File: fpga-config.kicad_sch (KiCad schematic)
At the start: 22 parts, among them J1 878321412, Q1 BSS138W-7-F, Q2 BSS138W-7-F, SW1 CVS-03B, U1 XC7K410T-2FFG900I, U2 TPD4E05U06QDQARQ1, U3 MAX1617AMEE+T

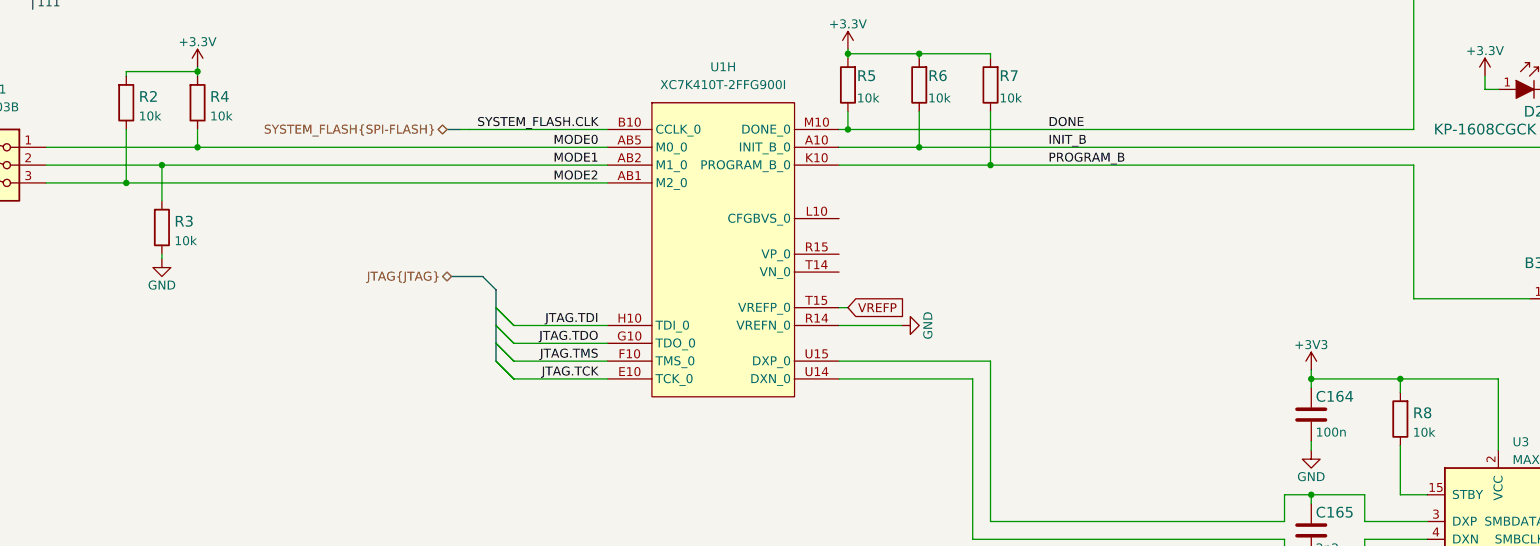
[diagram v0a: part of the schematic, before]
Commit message: Add new pinout to sup MCU. Start connecting it to FPGA
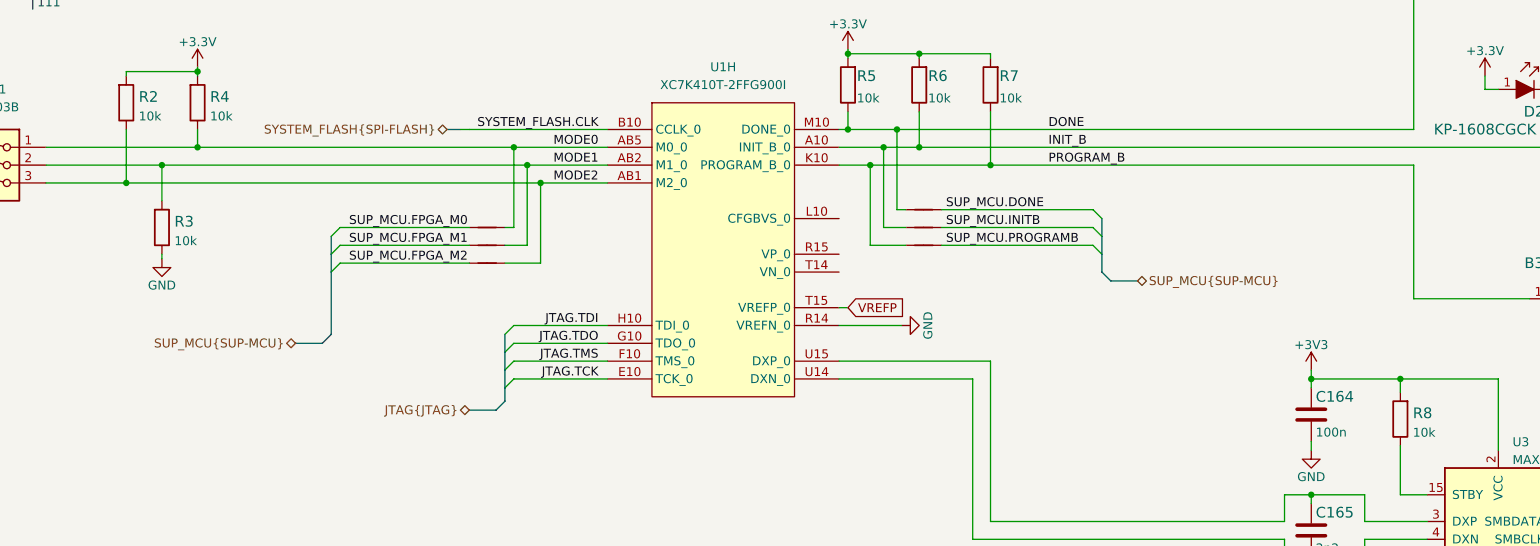
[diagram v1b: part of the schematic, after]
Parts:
- added NT? (x6): NetTie_2, antmicro-footprints:NetTie-2_SMD_Pad0.127mm, symbol antmicroShuntsJumpers:NetTie_2
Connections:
- net DONE: now also NT?.2
- net INIT_B: now also NT?.2
- net MODE0: now also NT?.2
- net MODE1: now also NT?.2
- net MODE2: now also NT?.2
- net PROGRAM_B: now also NT?.2
- new net SUP_MCU.DONE: NT?.1
- new net SUP_MCU.FPGA_M0: NT?.1
- new net SUP_MCU.FPGA_M1: NT?.1
- new net SUP_MCU.FPGA_M2: NT?.1
- new net SUP_MCU.INITB: NT?.1
- new net SUP_MCU.PROGRAMB: NT?.1

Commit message: Add DDR3L decoupling capacitors
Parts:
- gave numbers to parts that had none: 6
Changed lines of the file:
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@@
   (symbol (lib_id "antmicroShuntsJumpers:NetTie_2") (at 182.245 142.24 0) (unit 1)
     (in_bom yes) (on_board yes) (fields_autoplaced)
-    (property "Reference" "NT?" (id 0) (at 182.245 140.97 0)
+    (property "Reference" "NT3" (id 0) (at 182.245 140.97 0)
       (effects (font (size 1.27 1.27)) hide)
     )
@@
   (symbol (lib_id "antmicroShuntsJumpers:NetTie_2") (at 182.245 147.32 0) (unit 1)
     (in_bom yes) (on_board yes) (fields_autoplaced)
-    (property "Reference" "NT?" (id 0) (at 182.245 146.05 0)
+    (property "Reference" "NT5" (id 0) (at 182.245 146.05 0)
       (effects (font (size 1.27 1.27)) hide)
     )
@@
   (symbol (lib_id "antmicroShuntsJumpers:NetTie_2") (at 244.475 139.7 0) (mirror y) (unit 1)
     (in_bom yes) (on_board yes) (fields_autoplaced)
-    (property "Reference" "NT?" (id 0) (at 244.475 138.43 0)
+    (property "Reference" "NT6" (id 0) (at 244.475 138.43 0)
       (effects (font (size 1.27 1.27)) hide)
     )
@@
   (symbol (lib_id "antmicroShuntsJumpers:NetTie_2") (at 244.475 144.78 0) (mirror y) (unit 1)
     (in_bom yes) (on_board yes) (fields_autoplaced)
-    (property "Reference" "NT?" (id 0) (at 244.475 143.51 0)
+    (property "Reference" "NT8" (id 0) (at 244.475 143.51 0)
       (effects (font (size 1.27 1.27)) hide)
     )
@@
   (symbol (lib_id "antmicroShuntsJumpers:NetTie_2") (at 182.245 144.78 0) (unit 1)
     (in_bom yes) (on_board yes) (fields_autoplaced)
-    (property "Reference" "NT?" (id 0) (at 182.245 143.51 0)
+    (property "Reference" "NT4" (id 0) (at 182.245 143.51 0)
       (effects (font (size 1.27 1.27)) hide)
     )
@@
   (symbol (lib_id "antmicroShuntsJumpers:NetTie_2") (at 244.475 142.24 0) (mirror y) (unit 1)
     (in_bom yes) (on_board yes) (fields_autoplaced)
-    (property "Reference" "NT?" (id 0) (at 244.475 140.97 0)
-      (effects (font (size 1.27 1.27)) hide)
-    )
+    (property "Reference" "NT7" (id 0) (at 244.475 140.97 0)
+      (effects (font (size 1.27 1.27)) hide)
+    )

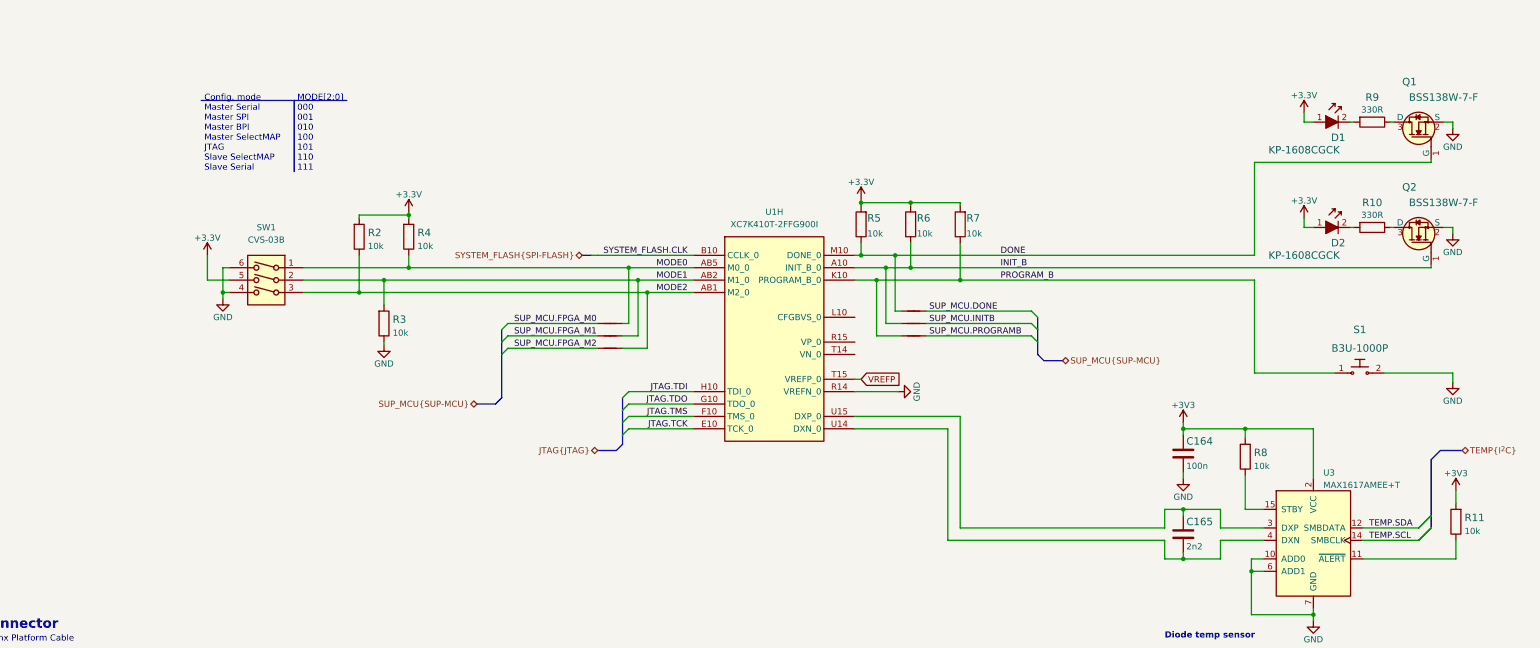
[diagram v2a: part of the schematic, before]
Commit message: Connect SUP MCU CLCK signal to FPGA
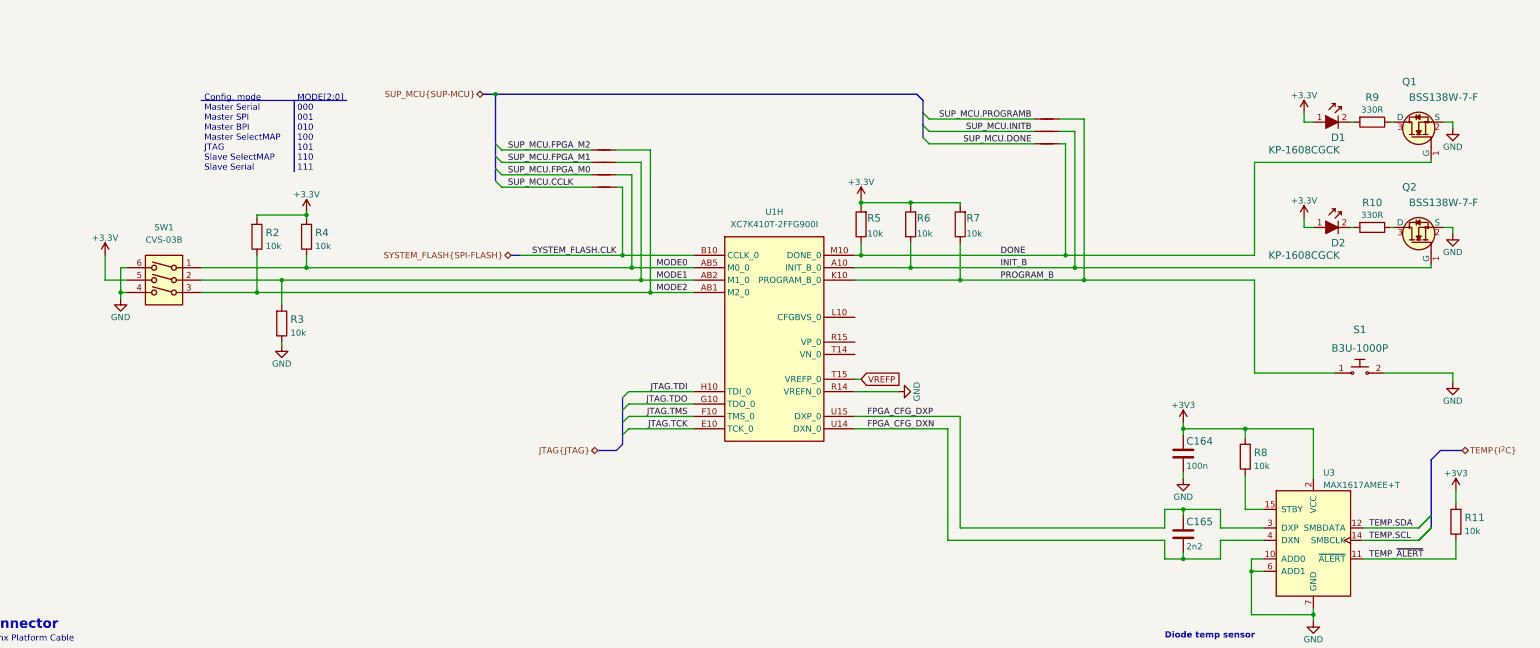
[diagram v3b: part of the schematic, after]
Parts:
- added NT?: NetTie_2, antmicro-footprints:NetTie-2_SMD_Pad0.127mm, symbol antmicroShuntsJumpers:NetTie_2
- renumbered NT3 to NT?, NT5 to NT?, NT6 to NT?, NT8 to NT?, NT4 to NT?, NT7 to NT?
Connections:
- net SYSTEM_FLASH.CLK: now also NT?.2
- net TEMP_~{ALERT}: now reaches R11.1, U3.11 (~{ALERT})
- net FPGA_CFG_DXP: now reaches C165.1, U1.U15 (DXP_0), U3.3 (DXP)
- net FPGA_CFG_DXN: now reaches C165.2, U1.U14 (DXN_0), U3.4 (DXN)
- new net SUP_MCU.CCLK: NT?.1
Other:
- moved on the sheet: R2, R3, R4, SW1

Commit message: Fix DDR3L placement
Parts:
- gave numbers to parts that had none: 7
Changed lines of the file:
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@@
   (symbol (lib_id "antmicroShuntsJumpers:NetTie_2") (at 180.975 111.76 0) (mirror x) (unit 1)
     (in_bom yes) (on_board yes) (fields_autoplaced)
-    (property "Reference" "NT?" (id 0) (at 180.975 113.03 0)
+    (property "Reference" "NT3" (id 0) (at 180.975 113.03 0)
       (effects (font (size 1.27 1.27)) hide)
     )
@@
   (symbol (lib_id "antmicroShuntsJumpers:NetTie_2") (at 180.975 114.3 0) (mirror x) (unit 1)
     (in_bom yes) (on_board yes) (fields_autoplaced)
-    (property "Reference" "NT?" (id 0) (at 180.975 115.57 0)
+    (property "Reference" "NT19" (id 0) (at 180.975 115.57 0)
       (effects (font (size 1.27 1.27)) hide)
     )
@@
   (symbol (lib_id "antmicroShuntsJumpers:NetTie_2") (at 180.975 106.68 0) (mirror x) (unit 1)
     (in_bom yes) (on_board yes) (fields_autoplaced)
-    (property "Reference" "NT?" (id 0) (at 180.975 107.95 0)
+    (property "Reference" "NT5" (id 0) (at 180.975 107.95 0)
       (effects (font (size 1.27 1.27)) hide)
     )
@@
   (symbol (lib_id "antmicroShuntsJumpers:NetTie_2") (at 271.78 105.41 0) (mirror x) (unit 1)
     (in_bom yes) (on_board yes) (fields_autoplaced)
-    (property "Reference" "NT?" (id 0) (at 271.78 106.68 0)
+    (property "Reference" "NT6" (id 0) (at 271.78 106.68 0)
       (effects (font (size 1.27 1.27)) hide)
     )
@@
   (symbol (lib_id "antmicroShuntsJumpers:NetTie_2") (at 271.78 100.33 0) (mirror x) (unit 1)
     (in_bom yes) (on_board yes) (fields_autoplaced)
-    (property "Reference" "NT?" (id 0) (at 271.78 101.6 0)
+    (property "Reference" "NT8" (id 0) (at 271.78 101.6 0)
       (effects (font (size 1.27 1.27)) hide)
     )
@@
   (symbol (lib_id "antmicroShuntsJumpers:NetTie_2") (at 180.975 109.22 0) (mirror x) (unit 1)
     (in_bom yes) (on_board yes) (fields_autoplaced)
-    (property "Reference" "NT?" (id 0) (at 180.975 110.49 0)
+    (property "Reference" "NT4" (id 0) (at 180.975 110.49 0)
       (effects (font (size 1.27 1.27)) hide)
     )
@@
   (symbol (lib_id "antmicroShuntsJumpers:NetTie_2") (at 271.78 102.87 0) (mirror x) (unit 1)
     (in_bom yes) (on_board yes) (fields_autoplaced)
-    (property "Reference" "NT?" (id 0) (at 271.78 104.14 0)
-      (effects (font (size 1.27 1.27)) hide)
-    )
+    (property "Reference" "NT7" (id 0) (at 271.78 104.14 0)
+      (effects (font (size 1.27 1.27)) hide)
+    )

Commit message: Finish connecting MCU
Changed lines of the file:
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@@
     (stroke (width 0) (type default) (color 0 0 0 0))
   )
-  (bus_entry (at 350.52 181.61) (size -2.54 2.54)
+  (bus_entry (at 350.52 182.88) (size -1.27 1.27)
     (stroke (width 0) (type default) (color 0 0 0 0))
   )
@@
     (stroke (width 0) (type default) (color 0 0 0 0))
   )
-  (bus_entry (at 350.52 181.61) (size -2.54 2.54)
-    (stroke (width 0) (type default) (color 0 0 0 0))
-  )
   (bus_entry (at 184.785 160.02) (size 1.27 -1.27)
     (stroke (width 0) (type default) (color 0 0 0 0))
@@
     (stroke (width 0) (type default) (color 0 0 0 0))
   )
-  (bus_entry (at 350.52 184.15) (size -2.54 2.54)
-    (stroke (width 0) (type default) (color 0 0 0 0))
-  )
   (bus_entry (at 86.36 229.87) (size -2.54 2.54)
     (stroke (width 0) (type default) (color 0 0 0 0))
   )
-  (bus_entry (at 350.52 184.15) (size -2.54 2.54)
+  (bus_entry (at 350.52 185.42) (size -1.27 1.27)
     (stroke (width 0) (type default) (color 0 0 0 0))
   )
@@
     (stroke (width 0) (type default) (color 0 0 0 0))
   )
-  (bus (pts (xy 350.52 181.61) (xy 350.52 184.15))
-    (stroke (width 0) (type default) (color 0 0 0 0))
-  )
   (wire (pts (xy 307.34 180.34) (xy 299.72 180.34))
     (stroke (width 0) (type default) (color 0 0 0 0))
@@
     (stroke (width 0) (type default) (color 0 0 0 0))
   )
-  (bus (pts (xy 350.52 170.18) (xy 350.52 181.61))
+  (bus (pts (xy 350.52 170.18) (xy 350.52 182.88))
     (stroke (width 0) (type default) (color 0 0 0 0))
   )
@@
     (stroke (width 0.1016) (type solid) (color 0 0 0 0))
   )
-  (wire (pts (xy 336.55 186.69) (xy 347.98 186.69))
+  (bus (pts (xy 350.52 182.88) (xy 350.52 185.42))
+    (stroke (width 0) (type default) (color 0 0 0 0))
+  )
+  (wire (pts (xy 336.55 186.69) (xy 349.25 186.69))
     (stroke (width 0) (type default) (color 0 0 0 0))
   )
@@
     (stroke (width 0) (type default) (color 0 0 0 0))
   )
-  (wire (pts (xy 336.55 184.15) (xy 347.98 184.15))
-    (stroke (width 0) (type default) (color 0 0 0 0))
-  )
+  (wire (pts (xy 336.55 184.15) (xy 349.25 184.15))
+    (stroke (width 0) (type default) (color 0 0 0 0))
+  )

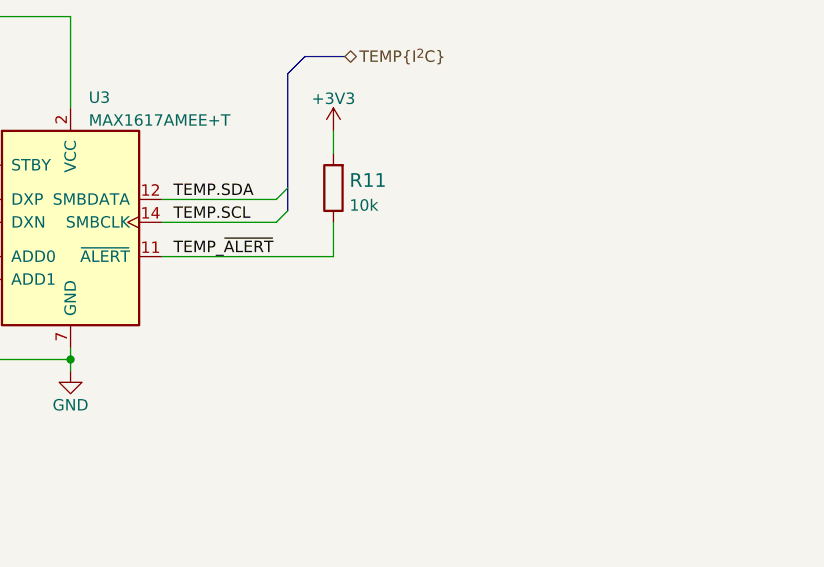
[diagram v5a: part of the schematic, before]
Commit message: Connect TEMP_ALERT_N signal to MCU
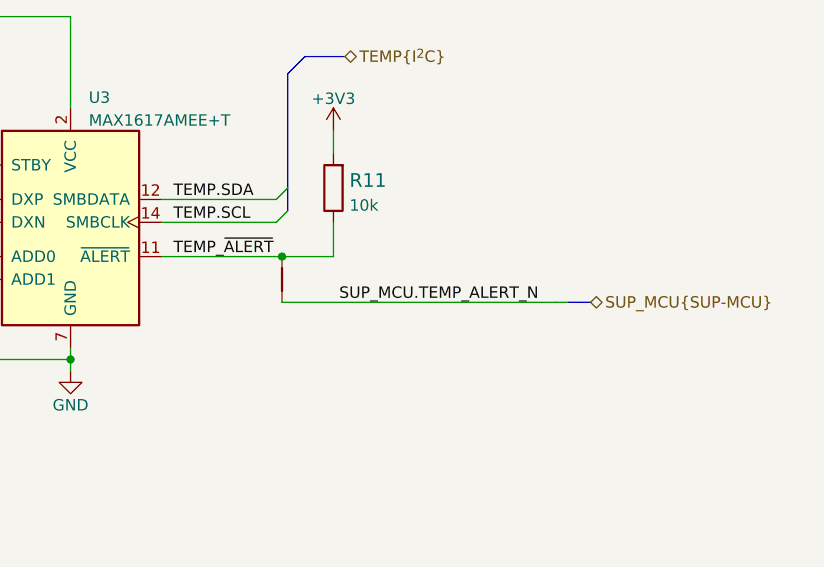
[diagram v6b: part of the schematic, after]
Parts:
- added NT?: NetTie_2, antmicro-footprints:NetTie-2_SMD_Pad0.127mm, symbol antmicroShuntsJumpers:NetTie_2
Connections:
- net TEMP_~{ALERT}: now also NT?.2
- new net SUP_MCU.TEMP_ALERT_N: NT?.1
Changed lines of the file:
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@@
   (junction (at 114.935 133.35) (diameter 0) (color 0 0 0 0)
+  )
+  (junction (at 349.885 190.5) (diameter 0) (color 0 0 0 0)
   )
   (junction (at 313.69 193.04) (diameter 0) (color 0 0 0 0)
@@
     (stroke (width 0) (type default) (color 0 0 0 0))
   )
+  (bus_entry (at 380.365 195.58) (size 1.27 0)
+    (stroke (width 0) (type default) (color 0 0 0 0))
+  )
   (bus_entry (at 158.75 113.03) (size 1.27 1.27)
     (stroke (width 0) (type default) (color 0 0 0 0))
@@
     (stroke (width 0) (type default) (color 0 0 0 0))
   )
-  (wire (pts (xy 336.55 190.5) (xy 355.6 190.5))
+  (wire (pts (xy 336.55 190.5) (xy 349.885 190.5))
     (stroke (width 0) (type default) (color 0 0 0 0))
   )
@@
     (stroke (width 0) (type default) (color 0 0 0 0))
   )
+  (wire (pts (xy 349.885 190.5) (xy 355.6 190.5))
+    (stroke (width 0) (type default) (color 0 0 0 0))
+  )
   (wire (pts (xy 334.645 122.555) (xy 334.01 122.555))
     (stroke (width 0) (type default) (color 0 0 0 0))
@@
   )
   (wire (pts (xy 66.04 229.87) (xy 83.82 229.87))
+    (stroke (width 0) (type default) (color 0 0 0 0))
+  )
+  (wire (pts (xy 349.885 195.58) (xy 380.365 195.58))
     (stroke (width 0) (type default) (color 0 0 0 0))
   )
@@
   )
   (wire (pts (xy 307.34 184.15) (xy 307.34 180.34))
+    (stroke (width 0) (type default) (color 0 0 0 0))
+  )
+  (bus (pts (xy 384.175 195.58) (xy 381.635 195.58))
     (stroke (width 0) (type default) (color 0 0 0 0))
   )
@@
   (label "MODE0" (at 198.12 130.81 180)
     (effects (font (size 1.27 1.27)) (justify right bottom))
+  )
+  (label "SUP_MCU.TEMP_ALERT_N" (at 356.235 195.58 0)
+    (effects (font (size 1.27 1.27)) (justify left bottom))
   )
   (label "JTAG.TCK" (at 73.025 227.33 0)
@@
   (hierarchical_label "SYSTEM_FLASH{SPI-FLASH}" (shape bidirectional) (at 161.925 128.27 180)
     (effects (font (size 1.27 1.27)) (justify right))
+  )
+  (hierarchical_label "SUP_MCU{SUP-MCU}" (shape bidirectional) (at 384.175 195.58 0)
+    (effects (font (size 1.27 1.27)) (justify left))
   )
   (symbol (lib_id "antmicroShuntsJumpers:NetTie_2") (at 180.975 111.76 0) (mirror x) (unit 1)
@@
     (pin "1")
   )
+  (symbol (lib_id "antmicroShuntsJumpers:NetTie_2") (at 349.885 193.04 270) (mirror x) (unit 1)
+    (in_bom yes) (on_board yes) (fields_autoplaced)
+    (property "Reference" "NT?" (id 0) (at 351.155 193.04 0)
+      (effects (font (size 1.27 1.27)) hide)
+    )
+    (property "Value" "NetTie_2" (id 1) (at 348.615 193.04 0)
+      (effects (font (size 1.27 1.27)) hide)
+    )
+    (property "Footprint" "antmicro-footprints:NetTie-2_SMD_Pad0.127mm" (id 2) (at 349.885 193.04 0)
+      (effects (font (size 1.27 1.27)) hide)
+    )
+    (property "Datasheet" "~" (id 3) (at 349.885 193.04 0)
+      (effects (font (size 1.27 1.27)) hide)
+    )
+    (pin "1")
+    (pin "2")
+  )
   (symbol (lib_id "antmicroShuntsJumpers:NetTie_2") (at 271.78 102.87 0) (mirror x) (unit 1)

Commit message: Fix libs, sync schematic with PCB
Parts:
- gave numbers to parts that had none: 1
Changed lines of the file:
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@@
   (symbol (lib_id "antmicroShuntsJumpers:NetTie_2") (at 349.885 193.04 270) (mirror x) (unit 1)
     (in_bom yes) (on_board yes) (fields_autoplaced)
-    (property "Reference" "NT?" (id 0) (at 351.155 193.04 0)
+    (property "Reference" "NT21" (id 0) (at 351.155 193.04 0)
       (effects (font (size 1.27 1.27)) hide)
     )
